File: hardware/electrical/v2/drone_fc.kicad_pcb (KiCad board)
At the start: 4 copper layers, 30 x 40.8 mm, 37 parts, among them J1 Cortex_SWD_10P, J2 ESC_4IN1_JST_SH, U1 TLV75533PDBVR, U2 LMR50410_Buck, U3 MDBT53-P1M, U4 ICM-42688-P

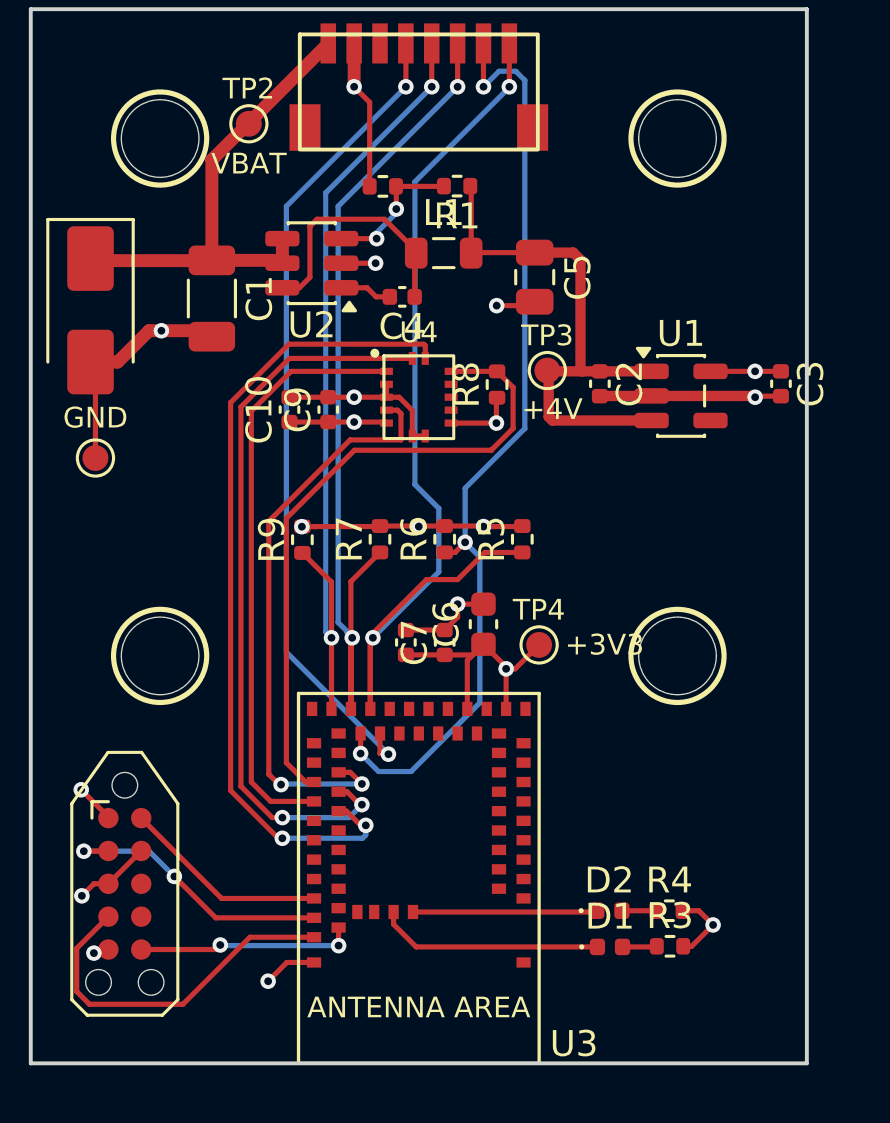
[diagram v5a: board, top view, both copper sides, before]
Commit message: layout: tidy silkscreen and clear the FB-to-SW clearance
Reworks the reference designators that sat over pads or ran off the board
outline, cutting the silkscreen findings from 23 to 5.

Also moves the feedback via clear of the buck switch node. It had come to
rest 0.10 mm from the SW track against a 0.20 mm rule - and SW is the
noisiest net on the board while FB is a high-impedance sense input, so the
coupling was worth removing properly rather than nudging to just inside the
limit.

The five remaining warnings are accepted: the U3 outline is clipped by the
board edge because the module is deliberately edge-aligned for its antenna,
and the J2 and U4 outlines cross their own pads in the footprints
themselves, which fabs clip against solder mask in production.
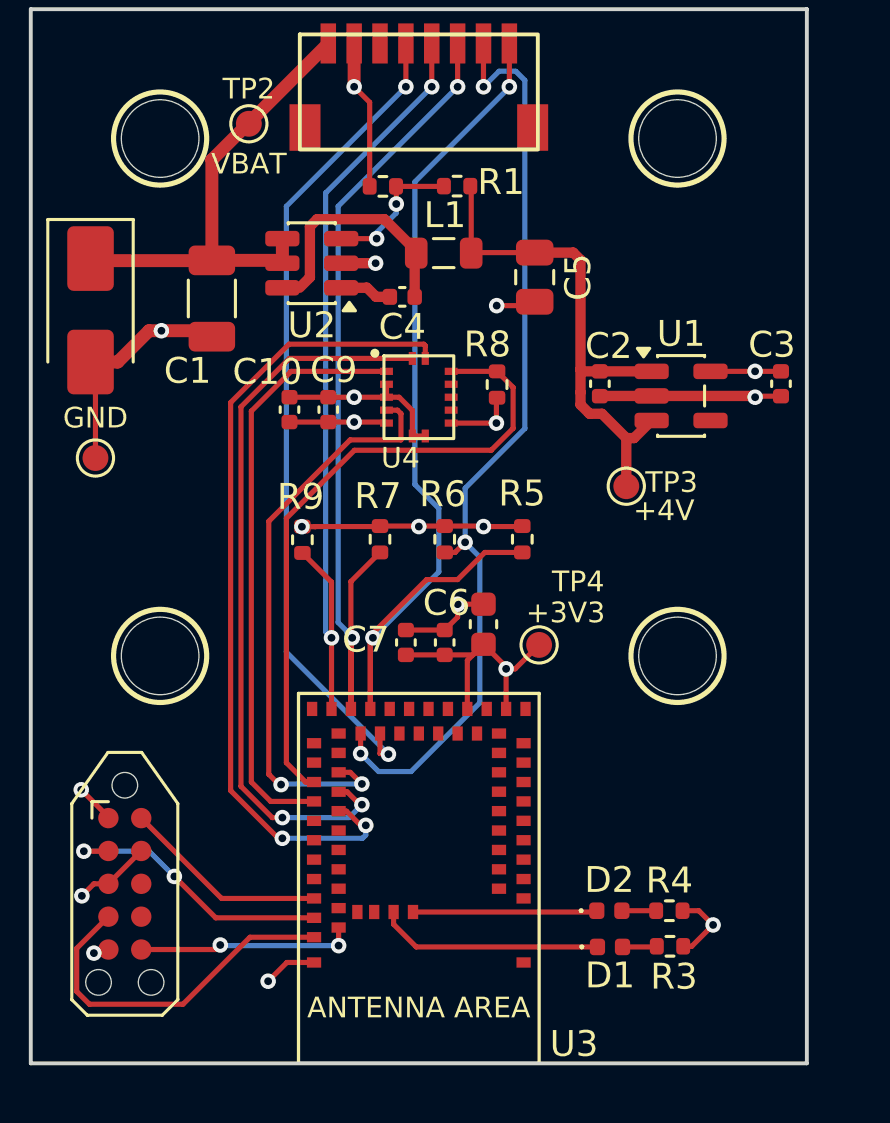
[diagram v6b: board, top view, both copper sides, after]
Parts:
- moved TP3 5.41 mm to (108.0, 103.4)
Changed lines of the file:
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@@
 		(tags "resistor")
 		(property "Reference" "R5"
-			(at 0 -1.17 90)
+			(at 1.77 -0.01 180)
 			(layer "F.SilkS")
 			(effects
@@
 		(tags "capacitor")
 		(property "Reference" "C7"
-			(at 0 -1.16 90)
+			(at 0.107836 -3.05 180)
 			(layer "F.SilkS")
 			(effects
@@
 		(tags "capacitor")
 		(property "Reference" "C3"
-			(at 0 -1.16 90)
+			(at -1.51 0.35 180)
 			(layer "F.SilkS")
 			(effects
@@
 		(tags "resistor")
 		(property "Reference" "R8"
-			(at 0 -1.17 90)
+			(at 1.55 -0.375 180)
 			(layer "F.SilkS")
 			(effects
@@
 		(at 104.65 109.575)
 		(property "Reference" "TP4"
-			(at 0 -1.35 0)
+			(at 1.51 -2.445 0)
 			(layer "F.SilkS")
 			(effects
@@
 		)
 		(fp_text user "+3V3"
-			(at 1 0 0)
+			(at -0.51 -1.245 0)
 			(layer "F.SilkS")
 			(effects
@@
 		(tags "capacitor")
 		(property "Reference" "C1"
-			(at 0 -1.85 90)
+			(at 2.795 0.94 180)
 			(layer "F.SilkS")
 			(effects
@@
 		(tags "resistor")
 		(property "Reference" "R1"
-			(at 0 -1.17 0)
+			(at -1.7 0.16 0)
 			(layer "F.SilkS")
 			(effects
@@
 		(tags "capacitor")
 		(property "Reference" "C9"
-			(at 0 -1.16 90)
+			(at 1.53 0.21 180)
 			(layer "F.SilkS")
 			(effects
@@
 		(tags "LED")
 		(property "Reference" "D1"
-			(at 0 -1.17 0)
+			(at 0 1.1 0)
 			(layer "F.SilkS")
 			(effects
@@
 		(tags "resistor")
 		(property "Reference" "R3"
-			(at 0 -1.17 0)
+			(at 0.153641 1.175 0)
 			(layer "F.SilkS")
 			(effects
@@
 		(tags "capacitor")
 		(property "Reference" "C10"
-			(at 0 -1.16 90)
+			(at 1.46 -0.85 180)
 			(layer "F.SilkS")
 			(effects
@@
 		(tags "LGA-14 IMU ICM-42688-P")
 		(property "Reference" "U4"
-			(at 0 -2.5 0)
+			(at -0.71 2.35 0)
 			(layer "F.SilkS")
 			(effects
@@
 		(tags "LED")
 		(property "Reference" "D2"
-			(at 0 -1.17 0)
+			(at 0 -1.19 0)
 			(layer "F.SilkS")
 			(effects
@@
 		(tags "resistor")
 		(property "Reference" "R7"
-			(at 0 -1.17 90)
+			(at 1.67 -0.08 180)
 			(layer "F.SilkS")
 			(effects
@@
 		(tags "resistor")
 		(property "Reference" "R6"
-			(at 0 -1.17 90)
+			(at 1.74 -0.07 180)
 			(layer "F.SilkS")
 			(effects
@@
 		(tags "capacitor")
 		(property "Reference" "C2"
-			(at 0 -1.16 90)
+			(at -1.46 -0.34 180)
 			(layer "F.SilkS")
 			(effects
@@
 	(footprint "TestPoint:TestPoint_Pad_D1.0mm"
 		(layer "F.Cu")
-		(at 104.97 98.97)
+		(at 108.02 103.44)
 		(property "Reference" "TP3"
-			(at 0 -1.35 0)
+			(at 1.75 -0.15 0)
 			(layer "F.SilkS")
 			(effects
@@
 		)
 		(fp_text user "+4V"
-			(at -1 1.5 0)
+			(at 0.27 0.94 0)
 			(layer "F.SilkS")
 			(effects
@@
 		(tags "resistor")
 		(property "Reference" "R9"
-			(at 0 -1.17 90)
+			(at 1.66 -0.07 180)
 			(layer "F.SilkS")
 			(effects
@@
 		(tags "capacitor")
 		(property "Reference" "C6"
-			(at 0 -1.43 90)
+			(at 0.825 -1.43 180)
 			(layer "F.SilkS")
 			(effects
@@
 		(tags "inductor")
 		(property "Reference" "L1"
-			(at 0 -1.55 0)
+			(at 0.0475 -1.47 0)
 			(layer "F.SilkS")
 			(effects
@@
 	)
 	(segment
+		(start 107.08 100.64)
+		(end 106.602444 100.64)
+		(width 0.4)
+		(layer "F.Cu")
+		(net "/+4V")
+	)
+	(segment
+		(start 106.32 99)
+		(end 107 99)
+		(width 0.4)
+		(layer "F.Cu")
+		(net "/+4V")
+	)
+	(segment
 		(start 104.48 94.41)
 		(end 102.045 94.41)
@@
 	)
 	(segment
+		(start 108.02 101.58)
+		(end 107.08 100.64)
+		(width 0.4)
+		(layer "F.Cu")
+		(net "/+4V")
+	)
+	(segment
 		(start 105.97 94.41)
 		(end 106.25 94.69)
@@
 	)
 	(segment
-		(start 105.02 100.76)
-		(end 105.02 99.02)
+		(start 104.48 94.41)
+		(end 105.97 94.41)
 		(width 0.4)
 		(layer "F.Cu")
@@
 	)
 	(segment
-		(start 104.48 94.41)
-		(end 105.97 94.41)
+		(start 106.25 100.287556)
+		(end 106.25 99.81)
 		(width 0.4)
 		(layer "F.Cu")
@@
 	)
 	(segment
-		(start 109 100.9)
-		(end 105.16 100.9)
+		(start 108.02 101.58)
+		(end 108.32 101.58)
 		(width 0.4)
 		(layer "F.Cu")
@@
 	)
 	(segment
-		(start 105.16 100.9)
-		(end 105.02 100.76)
+		(start 108.32 101.58)
+		(end 109 100.9)
+		(width 0.4)
+		(layer "F.Cu")
+		(net "/+4V")
+	)
+	(segment
+		(start 106.602444 100.64)
+		(end 106.25 100.287556)
+		(width 0.4)
+		(layer "F.Cu")
+		(net "/+4V")
+	)
+	(segment
+		(start 106.25 99.81)
+		(end 106.25 98.93)
 		(width 0.4)
 		(layer "F.Cu")
@@
 	)
 	(segment
-		(start 105 99)
-		(end 107 99)
+		(start 108.02 103.44)
+		(end 108.02 101.58)
 		(width 0.4)
 		(layer "F.Cu")
@@
 		(start 97 94.82)
 		(end 98.33 94.82)
-		(width 0.2)
+		(width 0.4)
 		(layer "F.Cu")
 		(net "GND")
@@
 		(start 97.98 95.77)
 		(end 97 95.77)
-		(width 0.2)
+		(width 0.4)
 		(layer "F.Cu")
 		(net "Net-(U2-BOOT)")
@@
 		(start 98.35 96.12)
 		(end 97.99 95.76)
-		(width 0.2)
+		(width 0.4)
 		(layer "F.Cu")
 		(net "Net-(U2-BOOT)")
@@
 		(start 98.88 96.12)
 		(end 98.35 96.12)
-		(width 0.2)
+		(width 0.4)
 		(layer "F.Cu")
 		(net "Net-(U2-BOOT)")
@@
 	)
 	(segment
-		(start 99.12919 92.727103)
-		(end 99.12919 91.85919)
+		(start 99.12 91.85)
+		(end 100.96 91.85)
 		(width 0.2)
 		(layer "F.Cu")
@@
 	)
 	(segment
-		(start 99.12 91.85)
-		(end 100.96 91.85)
+		(start 99.12919 92.53)
+		(end 99.12919 91.85919)
 		(width 0.2)
 		(layer "F.Cu")
@@
 	)
 	(via
-		(at 99.12919 92.727103)
+		(at 99.12919 92.53)
 		(size 0.6)
 		(drill 0.3)
@@
 	)
 	(segment
-		(start 99.135143 92.727103)
-		(end 99.207633 92.799593)
+		(start 99.12919 92.878036)
+		(end 98.37 93.637226)
 		(width 0.2)
 		(layer "B.Cu")
@@
 	)
 	(segment
-		(start 99.12919 92.727103)
-		(end 99.135143 92.727103)
+		(start 99.12919 92.53)
+		(end 99.135143 92.535953)
 		(width 0.2)
 		(layer "B.Cu")
@@
 	)
 	(segment
-		(start 99.12919 92.727103)
-		(end 99.12919 92.878036)
+		(start 99.135143 92.535953)
+		(end 99.135143 92.727103)
 		(width 0.2)
 		(layer "B.Cu")
@@
 	)
 	(segment
-		(start 99.12919 92.878036)
-		(end 98.37 93.637226)
+		(start 98.37 93.637226)
+		(end 98.37 93.87)
 		(width 0.2)
 		(layer "B.Cu")
@@
 	)
 	(segment
-		(start 98.37 93.637226)
-		(end 98.37 93.87)
+		(start 99.12919 92.53)
+		(end 99.12919 92.878036)
 		(width 0.2)
 		(layer "B.Cu")
@@
 		(start 96.067388 93.120102)
 		(end 96.499898 93.120102)
-		(width 0.2)
+		(width 0.4)
 		(layer "F.Cu")
 		(net "Net-(U2-SW)")
@@
 		(start 98.673557 93.12)
 		(end 99.9 94.346443)
-		(width 0.2)
+		(width 0.4)
 		(layer "F.Cu")
 		(net "Net-(U2-SW)")
@@
 		(start 99.84 96.12)
 		(end 99.84 94.49)
-		(width 0.2)
+		(width 0.4)
 		(layer "F.Cu")
 		(net "Net-(U2-SW)")
@@
 		(start 95.79 95.367499)
 		(end 95.79 93.39749)
-		(width 0.2)
+		(width 0.4)
 		(layer "F.Cu")
 		(net "Net-(U2-SW)")
@@
 		(start 96.5 93.12)
 		(end 98.673557 93.12)
-		(width 0.2)
+		(width 0.4)
 		(layer "F.Cu")
 		(net "Net-(U2-SW)")
@@
 		(start 95.387499 95.77)
 		(end 95.79 95.367499)
-		(width 0.2)
+		(width 0.4)
 		(layer "F.Cu")
 		(net "Net-(U2-SW)")
@@
 		(start 95.79 93.39749)
 		(end 96.067388 93.120102)
-		(width 0.2)
+		(width 0.4)
 		(layer "F.Cu")
 		(net "Net-(U2-SW)")
